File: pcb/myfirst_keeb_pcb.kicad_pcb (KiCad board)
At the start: 2 copper layers, 320.9 x 111.1 mm, 164 parts, among them J1 Conn_ARM_JTAG_SWD_10, Q1 DTC123J, SW1 SW_Push, SW3 Rotary_Encoder_Switch, U1 SRV05-4, U2 MCP1700-3302E_SOT23, U3 STM32F411RETx

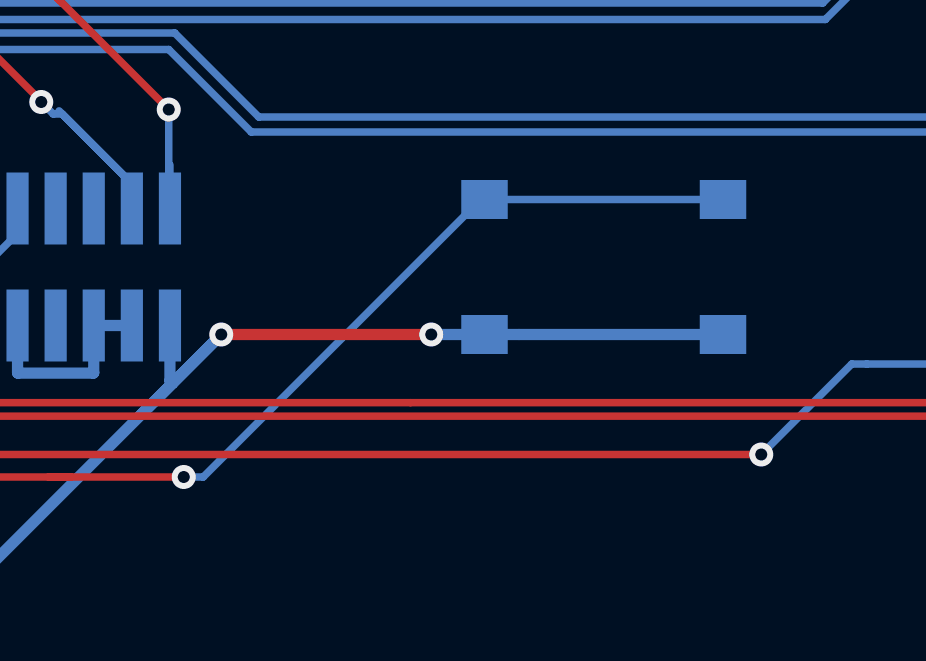
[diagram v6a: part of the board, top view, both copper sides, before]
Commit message: change boot button switch footprint - smaller and more available
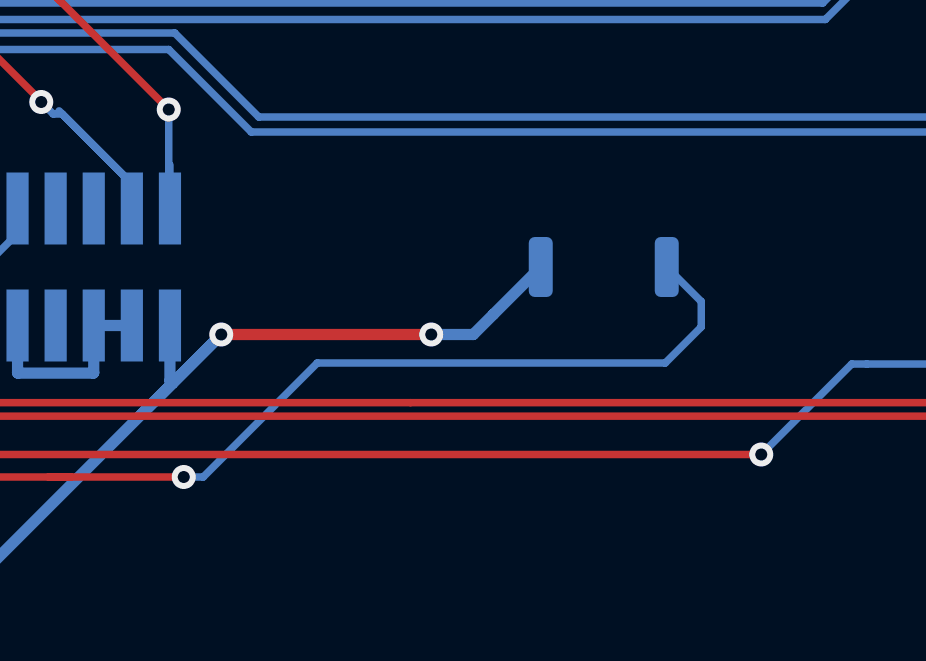
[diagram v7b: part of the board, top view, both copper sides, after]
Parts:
- SW1: footprint Button_Switch_SMD:SW_SPST_B3S-1000 -> Button_Switch_SMD:SW_Push_SPST_NO_Alps_SKRK
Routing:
- net +3V3: track 434.1 -> 428.9 mm
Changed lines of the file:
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@@
     (thickness 1.6)
     (drawings 2008)
-    (tracks 1232)
+    (tracks 1234)
     (zones 0)
     (modules 164)
@@
     (add_net VCC)
   )
+  (module Button_Switch_SMD:SW_Push_SPST_NO_Alps_SKRK (layer B.Cu)
+    (at 218.25 121.5 180)
+    (descr http://www.alps.com/prod/info/E/HTML/Tact/SurfaceMount/SKRK/SKRKAHE020.html)
+    (tags "SMD SMT button")
+    (attr smd)
+    (fp_text reference SW1 (at 0 2.25) (layer B.SilkS)
+      (effects (font (size 1 1) (thickness 0.15)) (justify mirror))
+    )
+    (fp_text value SW_Push (at 0 -2.5) (layer B.Fab)
+      (effects (font (size 1 1) (thickness 0.15)) (justify mirror))
+    )
+    (fp_line (start 2.07 1.57) (end 2.07 1.27) (layer B.SilkS) (width 0.12))
+    (fp_line (start -2.07 -1.57) (end -2.07 -1.27) (layer B.SilkS) (width 0.12))
+    (fp_line (start 1.95 1.45) (end 1.95 -1.45) (layer B.Fab) (width 0.1))
+    (fp_line (start -1.95 1.45) (end 1.95 1.45) (layer B.Fab) (width 0.1))
+    (fp_line (start -1.95 -1.45) (end -1.95 1.45) (layer B.Fab) (width 0.1))
+    (fp_line (start 1.95 -1.45) (end -1.95 -1.45) (layer B.Fab) (width 0.1))
+    (fp_line (start -2.75 -1.7) (end -2.75 1.7) (layer B.CrtYd) (width 0.05))
+    (fp_line (start 2.75 -1.7) (end -2.75 -1.7) (layer B.CrtYd) (width 0.05))
+    (fp_line (start 2.75 1.7) (end 2.75 -1.7) (layer B.CrtYd) (width 0.05))
+    (fp_line (start -2.75 1.7) (end 2.75 1.7) (layer B.CrtYd) (width 0.05))
+    (fp_text user %R (at 0 0) (layer B.Fab)
+      (effects (font (size 1 1) (thickness 0.15)) (justify mirror))
+    )
+    (fp_circle (center 0 0) (end 1 0) (layer B.Fab) (width 0.1))
+    (fp_line (start -2.07 1.27) (end -2.07 1.57) (layer B.SilkS) (width 0.12))
+    (fp_line (start 2.07 -1.57) (end -2.07 -1.57) (layer B.SilkS) (width 0.12))
+    (fp_line (start 2.07 -1.27) (end 2.07 -1.57) (layer B.SilkS) (width 0.12))
+    (fp_line (start -2.07 1.57) (end 2.07 1.57) (layer B.SilkS) (width 0.12))
+    (pad 1 smd roundrect (at -2.1 0 180) (size 0.8 2) (layers B.Cu B.Paste B.Mask) (roundrect_rratio 0.25)
+      (net 117 BOOT0))
+    (pad 2 smd roundrect (at 2.1 0 180) (size 0.8 2) (layers B.Cu B.Paste B.Mask) (roundrect_rratio 0.25)
+      (net 17 +3V3))
+    (model ${KISYS3DMOD}/Button_Switch_SMD.3dshapes/SW_Push_SPST_NO_Alps_SKRK.wrl
+      (at (xyz 0 0 0))
+      (scale (xyz 1 1 1))
+      (rotate (xyz 0 0 0))
+    )
+  )
   (module Type-C:HRO-TYPE-C-31-M-12-Assembly (layer B.Cu)
     (at 102.82428 28.3337)
@@
     )
   )
-  (module Button_Switch_SMD:SW_SPST_B3S-1000 (layer B.Cu)
-    (at 218.25 121.5 180)
-    (descr "Surface Mount Tactile Switch for High-Density Packaging")
-    (tags "Tactile Switch")
-    (attr smd)
-    (fp_text reference SW1 (at 0 4.5) (layer B.SilkS)
-      (effects (font (size 1 1) (thickness 0.15)) (justify mirror))
-    )
-    (fp_text value SW_Push (at 0 -4.5) (layer B.Fab)
-      (effects (font (size 1 1) (thickness 0.15)) (justify mirror))
-    )
-    (fp_line (start -3 -3.3) (end -3 3.3) (layer B.Fab) (width 0.1))
-    (fp_line (start 3 -3.3) (end -3 -3.3) (layer B.Fab) (width 0.1))
-    (fp_line (start 3 3.3) (end 3 -3.3) (layer B.Fab) (width 0.1))
-    (fp_line (start -3 3.3) (end 3 3.3) (layer B.Fab) (width 0.1))
-    (fp_circle (center 0 0) (end 1.65 0) (layer B.Fab) (width 0.1))
-    (fp_line (start 3.15 1.3) (end 3.15 -1.3) (layer B.SilkS) (width 0.12))
-    (fp_line (start -3.15 -3.45) (end -3.15 -3.2) (layer B.SilkS) (width 0.12))
-    (fp_line (start 3.15 -3.45) (end -3.15 -3.45) (layer B.SilkS) (width 0.12))
-    (fp_line (start 3.15 -3.2) (end 3.15 -3.45) (layer B.SilkS) (width 0.12))
-    (fp_line (start -3.15 -1.3) (end -3.15 1.3) (layer B.SilkS) (width 0.12))
-    (fp_line (start 3.15 3.45) (end 3.15 3.2) (layer B.SilkS) (width 0.12))
-    (fp_line (start -3.15 3.45) (end 3.15 3.45) (layer B.SilkS) (width 0.12))
-    (fp_line (start -3.15 3.2) (end -3.15 3.45) (layer B.SilkS) (width 0.12))
-    (fp_line (start -5 3.7) (end -5 -3.7) (layer B.CrtYd) (width 0.05))
-    (fp_line (start 5 3.7) (end -5 3.7) (layer B.CrtYd) (width 0.05))
-    (fp_line (start 5 -3.7) (end 5 3.7) (layer B.CrtYd) (width 0.05))
-    (fp_line (start -5 -3.7) (end 5 -3.7) (layer B.CrtYd) (width 0.05))
-    (fp_text user %R (at 0 4.5) (layer B.Fab)
-      (effects (font (size 1 1) (thickness 0.15)) (justify mirror))
-    )
-    (pad 2 smd rect (at 3.975 -2.25 180) (size 1.55 1.3) (layers B.Cu B.Paste B.Mask)
-      (net 17 +3V3))
-    (pad 2 smd rect (at -3.975 -2.25 180) (size 1.55 1.3) (layers B.Cu B.Paste B.Mask)
-      (net 17 +3V3))
-    (pad 1 smd rect (at 3.975 2.25 180) (size 1.55 1.3) (layers B.Cu B.Paste B.Mask)
-      (net 117 BOOT0))
-    (pad 1 smd rect (at -3.975 2.25 180) (size 1.55 1.3) (layers B.Cu B.Paste B.Mask)
-      (net 117 BOOT0))
-    (model ${KISYS3DMOD}/Button_Switch_SMD.3dshapes/SW_SPST_B3S-1000.wrl
-      (at (xyz 0 0 0))
-      (scale (xyz 1 1 1))
-      (rotate (xyz 0 0 0))
-    )
-  )
   (module Package_TO_SOT_SMD:SOT-23 (layer B.Cu)
     (at 167.25 124.5 180)
@@
   (segment (start 48.35652 83.77912) (end 47.68653 83.10913) (width 0.375) (layer B.Cu) (net 17))
   (via (at 212.5 123.75) (size 0.8) (drill 0.4) (layers F.Cu B.Cu) (net 17))
-  (segment (start 214.275 123.75) (end 212.5 123.75) (width 0.375) (layer B.Cu) (net 17))
   (via (at 205.5 123.75) (size 0.8) (drill 0.4) (layers F.Cu B.Cu) (net 17))
   (segment (start 212.5 123.75) (end 205.5 123.75) (width 0.375) (layer F.Cu) (net 17))
@@
   (segment (start 160.25 124.5) (end 160.25 123.934315) (width 0.375) (layer F.Cu) (net 17))
   (segment (start 158.575 114.325) (end 160.25 116) (width 0.375) (layer F.Cu) (net 17))
-  (segment (start 215.425 123.75) (end 222.225 123.75) (width 0.375) (layer B.Cu) (net 17))
-  (segment (start 214.275 123.75) (end 215.425 123.75) (width 0.375) (layer B.Cu) (net 17))
   (via (at 155.5968 114.24736) (size 0.8) (drill 0.4) (layers F.Cu B.Cu) (net 17))
   (segment (start 158.575 114.325) (end 155.67444 114.325) (width 0.375) (layer F.Cu) (net 17))
@@
   (segment (start 146.75 125.675) (end 146.75 128.5) (width 0.25) (layer B.Cu) (net 17))
   (segment (start 71.46036 33.3248) (end 73.27388 35.13832) (width 0.375) (layer B.Cu) (net 17))
+  (segment (start 213.9 123.75) (end 214.575 123.075) (width 0.375) (layer B.Cu) (net 17))
+  (segment (start 212.5 123.75) (end 213.9 123.75) (width 0.375) (layer B.Cu) (net 17))
+  (segment (start 214.575 123.075) (end 216.15 121.5) (width 0.375) (layer B.Cu) (net 17))
   (segment (start 93.23578 36.02736) (end 89.15146 36.02736) (width 0.25) (layer B.Cu) (net 18))
   (segment (start 89.0905 32.94126) (end 89.15146 32.8803) (width 0.25) (layer B.Cu) (net 18))
@@
   (segment (start 170.5 123.5) (end 175.5 128.5) (width 0.25) (layer B.Cu) (net 117))
   (segment (start 175.5 128.5) (end 179.996118 128.5) (width 0.25) (layer B.Cu) (net 117))
-  (segment (start 222.225 119.25) (end 214.275 119.25) (width 0.25) (layer B.Cu) (net 117))
-  (segment (start 214.15 119.25) (end 204.9 128.5) (width 0.25) (layer B.Cu) (net 117))
-  (segment (start 214.275 119.25) (end 214.15 119.25) (width 0.25) (layer B.Cu) (net 117))
   (via (at 204.25 128.5) (size 0.8) (drill 0.4) (layers F.Cu B.Cu) (net 117))
-  (segment (start 204.9 128.5) (end 204.25 128.5) (width 0.25) (layer B.Cu) (net 117))
   (segment (start 204.25 128.5) (end 199.75 128.5) (width 0.25) (layer F.Cu) (net 117))
   (segment (start 189.25 128.5) (end 199.75 128.5) (width 0.25) (layer F.Cu) (net 117))
   (segment (start 199.75 128.5) (end 200.5 128.5) (width 0.25) (layer F.Cu) (net 117))
   (segment (start 154.675 121.75) (end 163.75 121.75) (width 0.25) (layer B.Cu) (net 117))
+  (segment (start 221.5 122.65) (end 220.35 121.5) (width 0.25) (layer B.Cu) (net 117))
+  (segment (start 221.5 123.5) (end 221.5 122.65) (width 0.25) (layer B.Cu) (net 117))
+  (segment (start 220.3 124.7) (end 221.5 123.5) (width 0.25) (layer B.Cu) (net 117))
+  (segment (start 208.7 124.7) (end 220.3 124.7) (width 0.25) (layer B.Cu) (net 117))
+  (segment (start 204.25 128.5) (end 204.9 128.5) (width 0.25) (layer B.Cu) (net 117))
+  (segment (start 204.9 128.5) (end 208.7 124.7) (width 0.25) (layer B.Cu) (net 117))
   (zone (net 104) (net_name GND) (layer F.Cu) (hatch edge 0.508)
     (connect_pads (clearance 0.508))

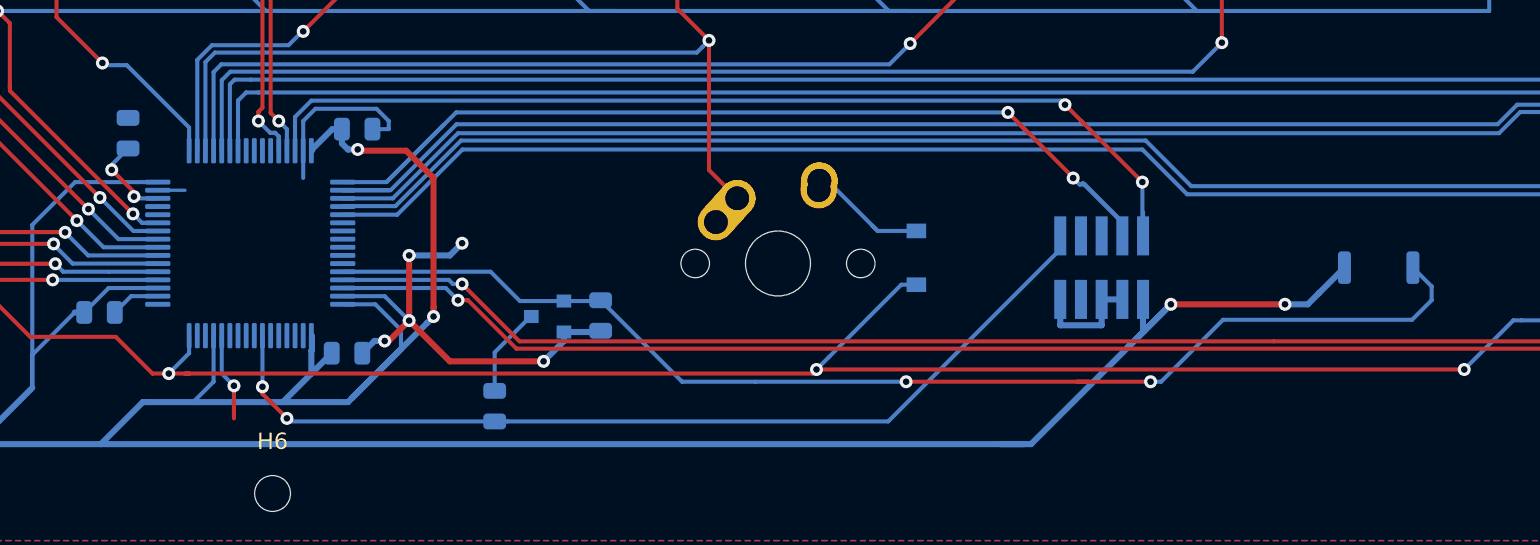
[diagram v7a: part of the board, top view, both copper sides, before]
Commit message: flip boot switch and jtag conn to top
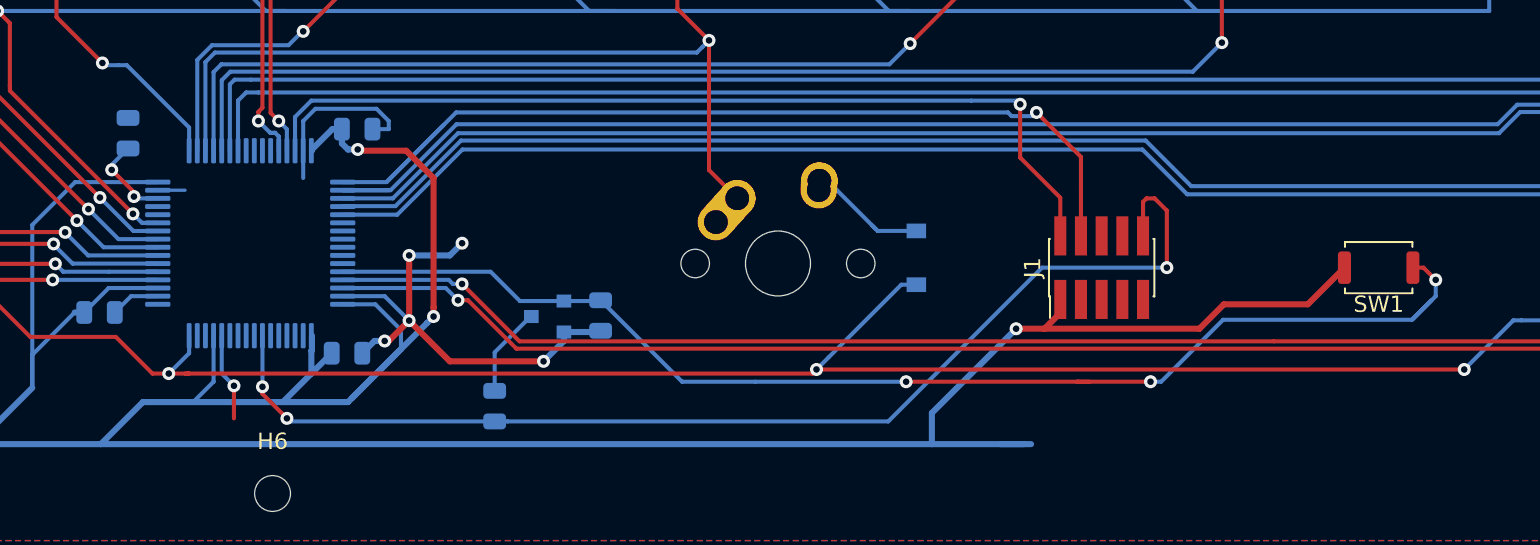
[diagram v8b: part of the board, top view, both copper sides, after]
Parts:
- J1, SW1: moved to F.Cu
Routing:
- net NRST: track 58.4 -> 71.1 mm, vias 2 -> 3
- net GND: track 340.8 -> 333.8 mm
- net SWDIO: track 61.5 -> 56.2 mm, vias 2 -> 1
- net +3V3: track 428.9 -> 432.6 mm, vias 4 -> 3
- net SWDCLK: track 62.0 -> 58.5 mm, vias 2 -> 1
- net BOOT0: track 75.0 -> 77.1 mm, vias 2 -> 3
